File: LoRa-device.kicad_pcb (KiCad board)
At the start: 4 copper layers, 86.4 x 50.8 mm, 114 parts, among them J1 Connector, USB-TYPE-C-16P, J2 Conn_01x02_Pin, J3 Conn_Coaxial, J4 Conn_01x14_Pin, J6 Conn_01x04_Pin, J7 Screw_Terminal_01x08, J8 U.FL, Q1 AO3401A, Q2 S8050, SW1 SW_Nidec_CAS-120A1, U1 ESP32-S3, U11 L76KB-A58, U2 W25Q128JVS, U3 TP4055, U4 ATECC608A-SSHDA, U5 Ai-Thinker-Ra-01, U6 USBLC6-2P6, U8 TPS22917LDBV, U9 AP63203WU, Y1 32.768 kHz, Y2 40MHz(10ppm)

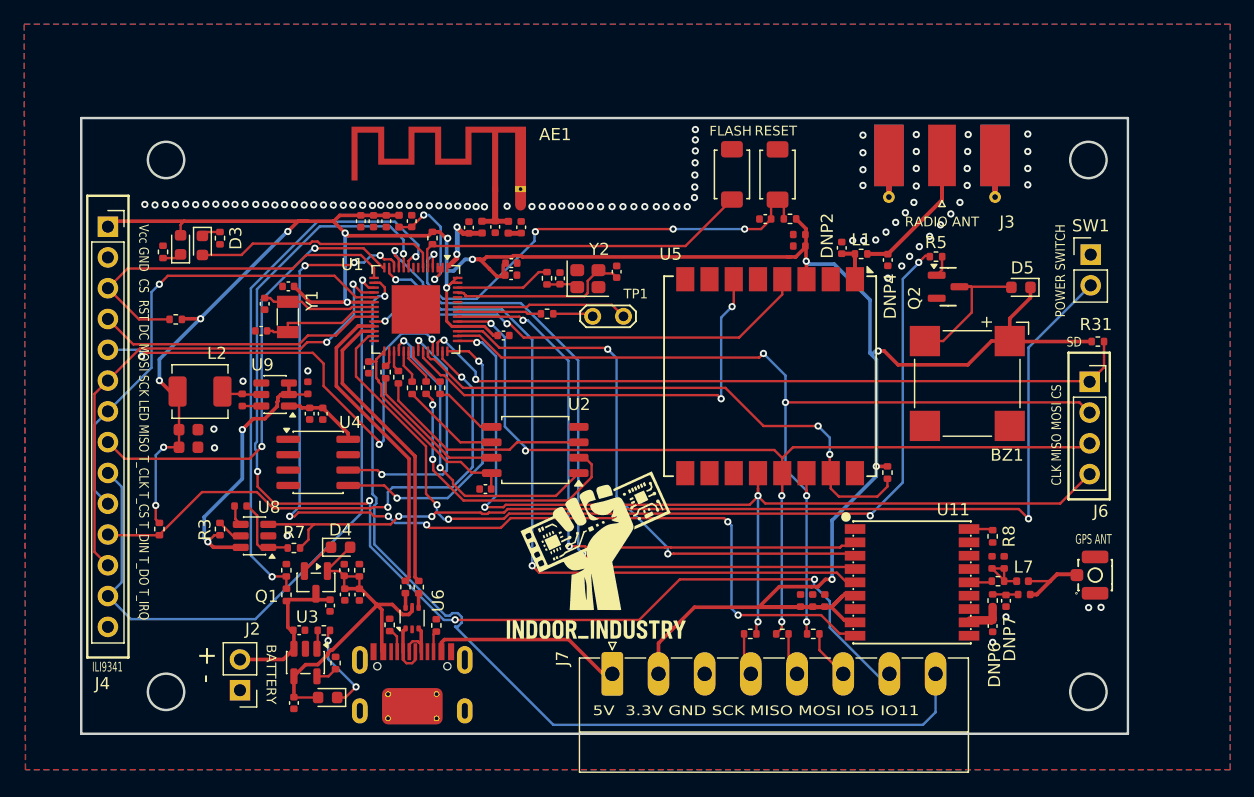
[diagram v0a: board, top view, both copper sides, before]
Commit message: 3d model, case space for battery.
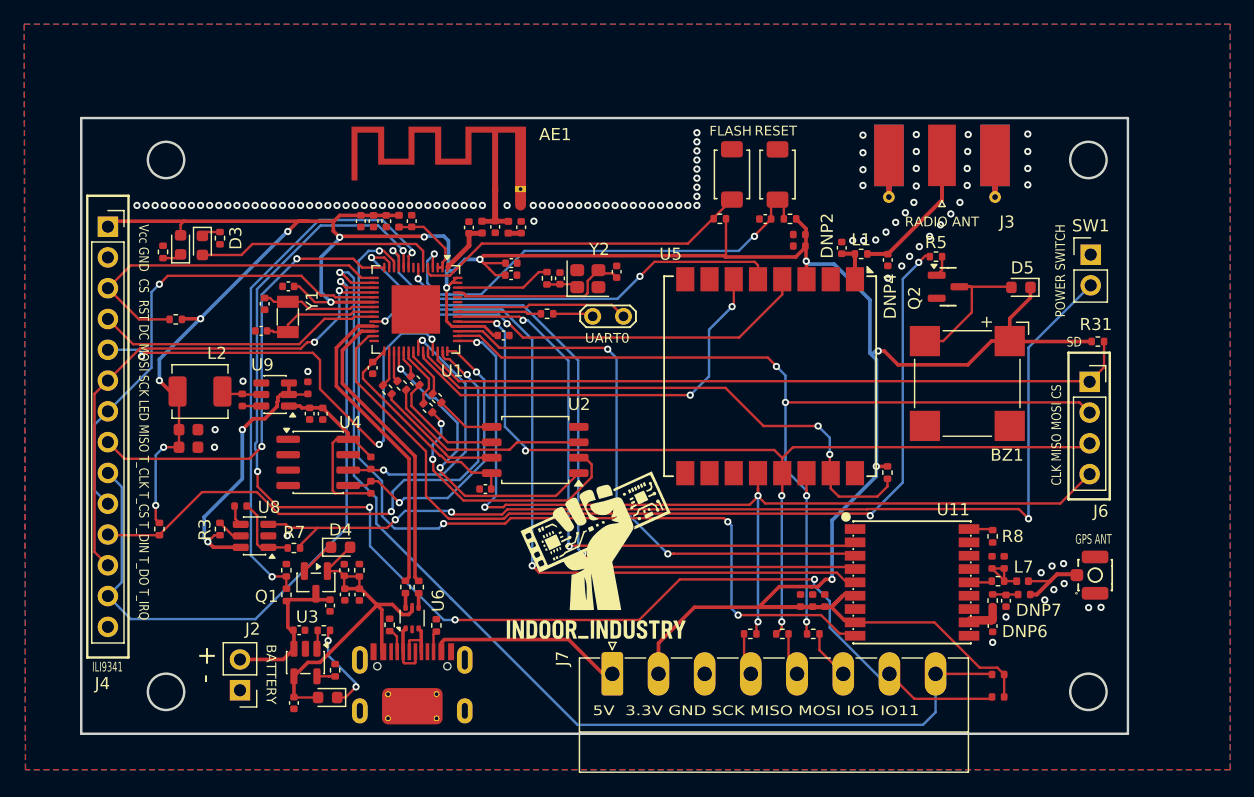
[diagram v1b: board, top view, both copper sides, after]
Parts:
- added R35: 4.7kΩ, PCM_JLCPCB:R_0402, F.Cu at (177.6, 121.6)
- added R37: 4.7kΩ, PCM_JLCPCB:R_0402, F.Cu at (177.6, 119.8)
- added R4: 4.7kΩ, PCM_JLCPCB:R_0402, F.Cu at (125.8, 102.3)
- added R6: 4.7kΩ, PCM_JLCPCB:R_0402, F.Cu at (125.8, 104.3)
- moved R21 23.8 mm to (154.6, 82.2), turned to 180 degrees
- moved R27 1.67 mm to (130.5, 97.8), turned to -45 degrees
- moved R30 1.46 mm to (127.2, 96.2), turned to -45 degrees
- moved R26 0.90 mm to (131.2, 97.0), turned to -45 degrees
- moved R29 0.74 mm to (128.3, 95.9), turned to -45 degrees
- moved R28 0.65 mm to (129.4, 95.5), turned to -45 degrees
- moved R1 0.60 mm to (122.8, 119.4)
- moved C13 0.33 mm to (126.0, 94.5)
- renumbered TP1 to UART0
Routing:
- net IO2: track 0.51 -> 32.8 mm, vias 0 -> 2
- net VDD_CPU: track 245.6 -> 277.0 mm
- net IO7: track 85.0 -> 73.6 mm, vias 8 -> 4
- net IO5: track 99.2 -> 107.6 mm
- net IO11: track 80.0 -> 86.3 mm
- net Net-(C19-Pad1): track 10.3 -> 6.63 mm, vias 2 -> 0
- net IO8: track 60.4 -> 63.9 mm
- net Net-(U1-SPIQ): track 3.10 -> 5.19 mm
- net IO47: track 37.5 -> 35.5 mm
- net VDD_SPI: track 17.8 -> 19.5 mm
- net Net-(U1-SPIHD): track 1.33 -> 3.03 mm
- net SPISCK: track 8.24 -> 9.90 mm
- net SPIHD: track 12.2 -> 10.7 mm
- net IO48: track 21.0 -> 22.5 mm
- net MISOB: track 57.0 -> 58.4 mm
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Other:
- board text added: "BAT"

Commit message: External header protection, clean routing
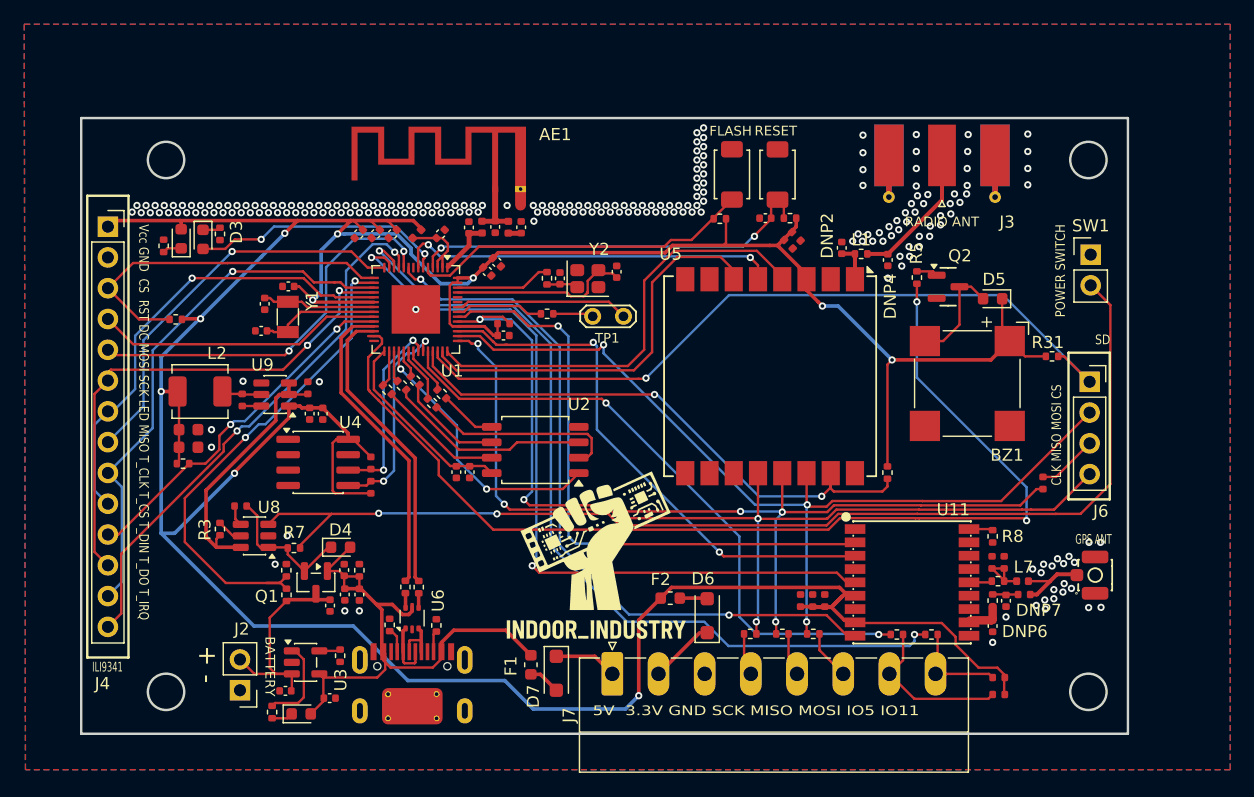
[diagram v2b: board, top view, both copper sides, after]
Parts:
- added D6: PMEG2010AEH, Diode_SMD:D_SOD-123F, F.Cu at (153.6, 114.9)
- added D7: PMEG2010AEH, Diode_SMD:D_SOD-123F, F.Cu at (141.1, 119.7)
- added F1: Polyfuse, Fuse:Fuse_0603_1608Metric, F.Cu at (139.0, 119.0)
- added F2: Polyfuse, Fuse:Fuse_0603_1608Metric, F.Cu at (150.5, 113.5)
- added R38: 10Ω, Resistor_SMD:R_0402_1005Metric, F.Cu at (172.1, 116.5)
- added R39: 10Ω, Resistor_SMD:R_0402_1005Metric, F.Cu at (169.2, 116.5)
- added R40: 100kΩ, PCM_JLCPCB:R_0402, F.Cu at (136.8, 90.8)
- added R41: 47Ω, PCM_JLCPCB:R_0402, F.Cu at (181.2, 104.0)
- moved C13 11.0 mm to (132.8, 103.0)
- moved R15 7.98 mm to (117.7, 122.8), turned to -90 degrees
- moved R11 5.74 mm to (110.3, 102.3), turned to 0 degrees
- moved C2 5.13 mm to (118.8, 121.1), turned to 180 degrees
- moved R31 3.97 mm to (182.0, 93.5)
- moved C1 2.98 mm to (122.4, 121.7), turned to 0 degrees
- moved C19 2.61 mm to (131.6, 83.4), turned to 45 degrees
- moved D1 2.57 mm to (120.0, 123.0), turned to 0 degrees
- moved D5 2.52 mm to (177.1, 88.8)
- moved R5 2.34 mm to (170.8, 87.0), turned to 90 degrees
- moved C39 2.11 mm to (135.4, 86.5), turned to -45 degrees
- moved C32 1.91 mm to (133.9, 103.0), turned to -90 degrees
- moved L3 1.81 mm to (129.6, 83.4), turned to -135 degrees
- moved C40 1.59 mm to (136.2, 85.7), turned to -45 degrees
- moved R1 1.27 mm to (123.3, 118.2), turned to 90 degrees
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- renumbered UART0 to TP1
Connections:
- J4 pad 11: IO36 -> IO18
- J4 pad 14: unconnected-(J4-Pin_14-Pad14) -> IO6
- J4 pad 5: IO34 -> IO5
- J6 pad 3: MISOA -> Net-(J6-Pin_3)
- J7 pad 1: 5V -> Net-(D7-K)
- J7 pad 2: VDD_CPU -> Net-(D6-K)
- J7 pad 7: IO5 -> Net-(J7-Pin_7)
- J7 pad 8: IO11 -> Net-(J7-Pin_8)
- R10 pad 2: IO33 -> IO34
- R11 pad 2: IO36 -> IO18
- R12 pad 2: IO4/BAT -> IO11/BAT
- R19 pad 1: IO4/BAT -> IO11/BAT
- R35 pad 2: IO5 -> Net-(J7-Pin_7)
- R37 pad 2: IO11 -> Net-(J7-Pin_8)
- R6 pad 2: IO37 -> IO47
- U1 pad 16: IO11 -> IO11/BAT
- U1 pad 9: IO4/BAT -> IO4
- U11 pad 4: IO6 -> unconnected-(U11-1PPS-Pad4)
- U11 pad 9: IO7 -> IO4
- U4 pad 5: IO37 -> IO47
- U5 pad 15: IO33 -> IO34
- U5 pad 4: IO18 -> IO37
- U5 pad 6: IO47 -> IO36
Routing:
- net IO11: track 86.3 -> 0.00 mm, vias 1 -> 0
- net IO5: track 107.6 -> 32.7 mm, vias 5 -> 2
- net IO4: track 0.00 -> 59.5 mm, vias 0 -> 2
- net IO4/BAT: track 45.1 -> 0.00 mm, vias 2 -> 0
- net IO11/BAT: track 0.00 -> 41.4 mm, vias 0 -> 2
- net VDD_CPU: track 277.0 -> 314.8 mm, vias 14 -> 10
- net IO47: track 35.5 -> 17.3 mm
- net IO6: track 60.3 -> 44.5 mm
- net MISOB: track 58.4 -> 44.3 mm
- net Net-(J7-Pin_7): track 0.00 -> 13.2 mm
- net IO37: track 24.4 -> 36.8 mm, vias 2 -> 0
- net IO21: track 77.9 -> 89.5 mm
- net IO36: track 46.2 -> 34.7 mm, vias 2 -> 0
- net Net-(J7-Pin_8): track 0.00 -> 8.15 mm
- net IO18: track 37.5 -> 30.0 mm
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
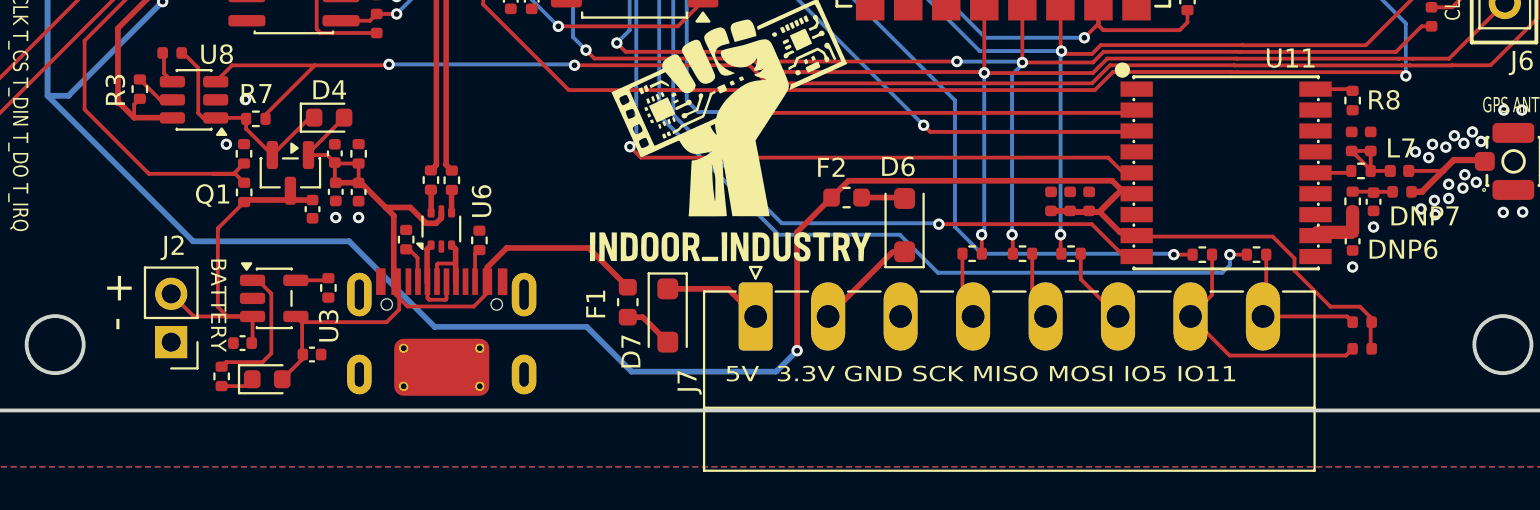
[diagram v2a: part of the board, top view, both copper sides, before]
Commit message: L76K V_BCKP added
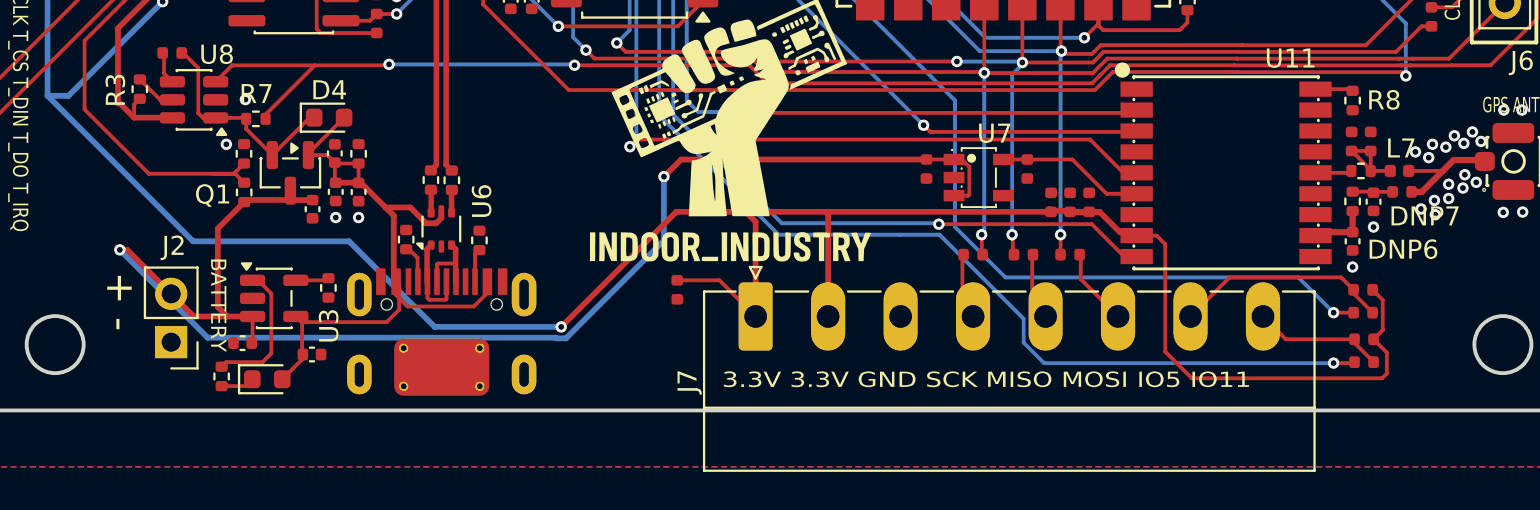
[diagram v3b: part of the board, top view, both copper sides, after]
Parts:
- removed D6, D7: PMEG2010AEH, Diode_SMD:D_SOD-123F
- removed F1, F2: Polyfuse, Fuse:Fuse_0603_1608Metric
- removed R32, R33, R34, R38, R39: 10Ω, Resistor_SMD:R_0402_1005Metric
- added C30: 1uF, PCM_JLCPCB:C_0402, F.Cu at (141.6, 118.3)
- added C34: 1uF, PCM_JLCPCB:C_0402, F.Cu at (160.0, 112.0)
- added C41: 1uF, PCM_JLCPCB:C_0402, F.Cu at (154.7, 112.0)
- added R42: 100Ω, PCM_JLCPCB:R_0402, F.Cu at (162.2, 116.5)
- added R43: 100Ω, PCM_JLCPCB:R_0402, F.Cu at (177.7, 122.1)
- added R44: 100Ω, PCM_JLCPCB:R_0402, F.Cu at (177.7, 119.5)
- added R45: 100Ω, PCM_JLCPCB:R_0402, F.Cu at (159.8, 116.5)
- added R46: 100Ω, PCM_JLCPCB:R_0402, F.Cu at (157.2, 116.5)
- added U7: STLQ015M33R, Lora-device:SOT-23-5_L3.0-W1.7-P0.95-LS2.8-BR, F.Cu at (157.4, 112.4)
- moved R35 3.10 mm to (177.7, 118.3)
- moved R37 0.91 mm to (177.7, 120.9)
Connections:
- J7 pad 1: Net-(D7-K) -> VDD_CPU
- J7 pad 2: Net-(D6-K) -> VDD_CPU
- U11 pad 6: VDD_CPU -> Net-(U11-V_BCKP)
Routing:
- net VBAT: track 18.4 -> 77.0 mm, vias 0 -> 2
- net IO33: track 52.5 -> 62.2 mm
- net VDD_CPU: track 314.8 -> 324.5 mm
- net 5V: track 46.1 -> 36.6 mm
- net Net-(U11-V_BCKP): track 0.00 -> 8.35 mm
- net IO7: track 71.1 -> 78.9 mm
- net Net-(D6-K): track 5.99 -> 0.00 mm
- net Net-(D7-K): track 5.22 -> 0.00 mm
- net Net-(D7-A): track 2.64 -> 0.00 mm
- net Net-(D6-A): track 2.28 -> 0.00 mm
- net Net-(J7-Pin_7): track 13.2 -> 11.5 mm
- net Net-(J7-Pin_8): track 8.15 -> 7.17 mm
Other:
- board text added: "3.3V 3.3V GND SCK MISO MOSI IO5 IO11"
- board text removed: "5V 3.3V GND SCK MISO MOSI IO5 IO11"
